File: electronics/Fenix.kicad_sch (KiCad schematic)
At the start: 9 parts, among them J1 PWR, J2 RELAY_CTRL

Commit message: Update Symbol/Footprint link & Remove GPS board
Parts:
- removed U5: (no value), Parts:Adafruit_GPSFeather, symbol Parts:Adafruit_GPSWing
- renumbered U1 to Gyro1, U3 to LoRa32_V1, U2 to Servo_Controller1, U4 to uSD1
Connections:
- net +3V3: now also TEMP_EXT1.1 (VIN), TEMP_INT1.1 (VIN); no longer TEMP_EXT1.01 (VIN), TEMP_INT1.01 (VIN)
- net GND: now also TEMP_EXT1.2 (GND), TEMP_INT1.2 (GND); no longer TEMP_EXT1.02 (GND), TEMP_INT1.02 (GND)
- net I2C_CLK: now also TEMP_EXT1.3 (SCL), TEMP_INT1.3 (SCL); no longer TEMP_EXT1.03 (SCL), TEMP_INT1.03 (SCL)
- net I2C_DATA: now also TEMP_EXT1.4 (SDA), TEMP_INT1.4 (SDA); no longer TEMP_EXT1.04 (SDA), TEMP_INT1.04 (SDA)
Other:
- note removed: "GPS & Real-Time Clock Module"

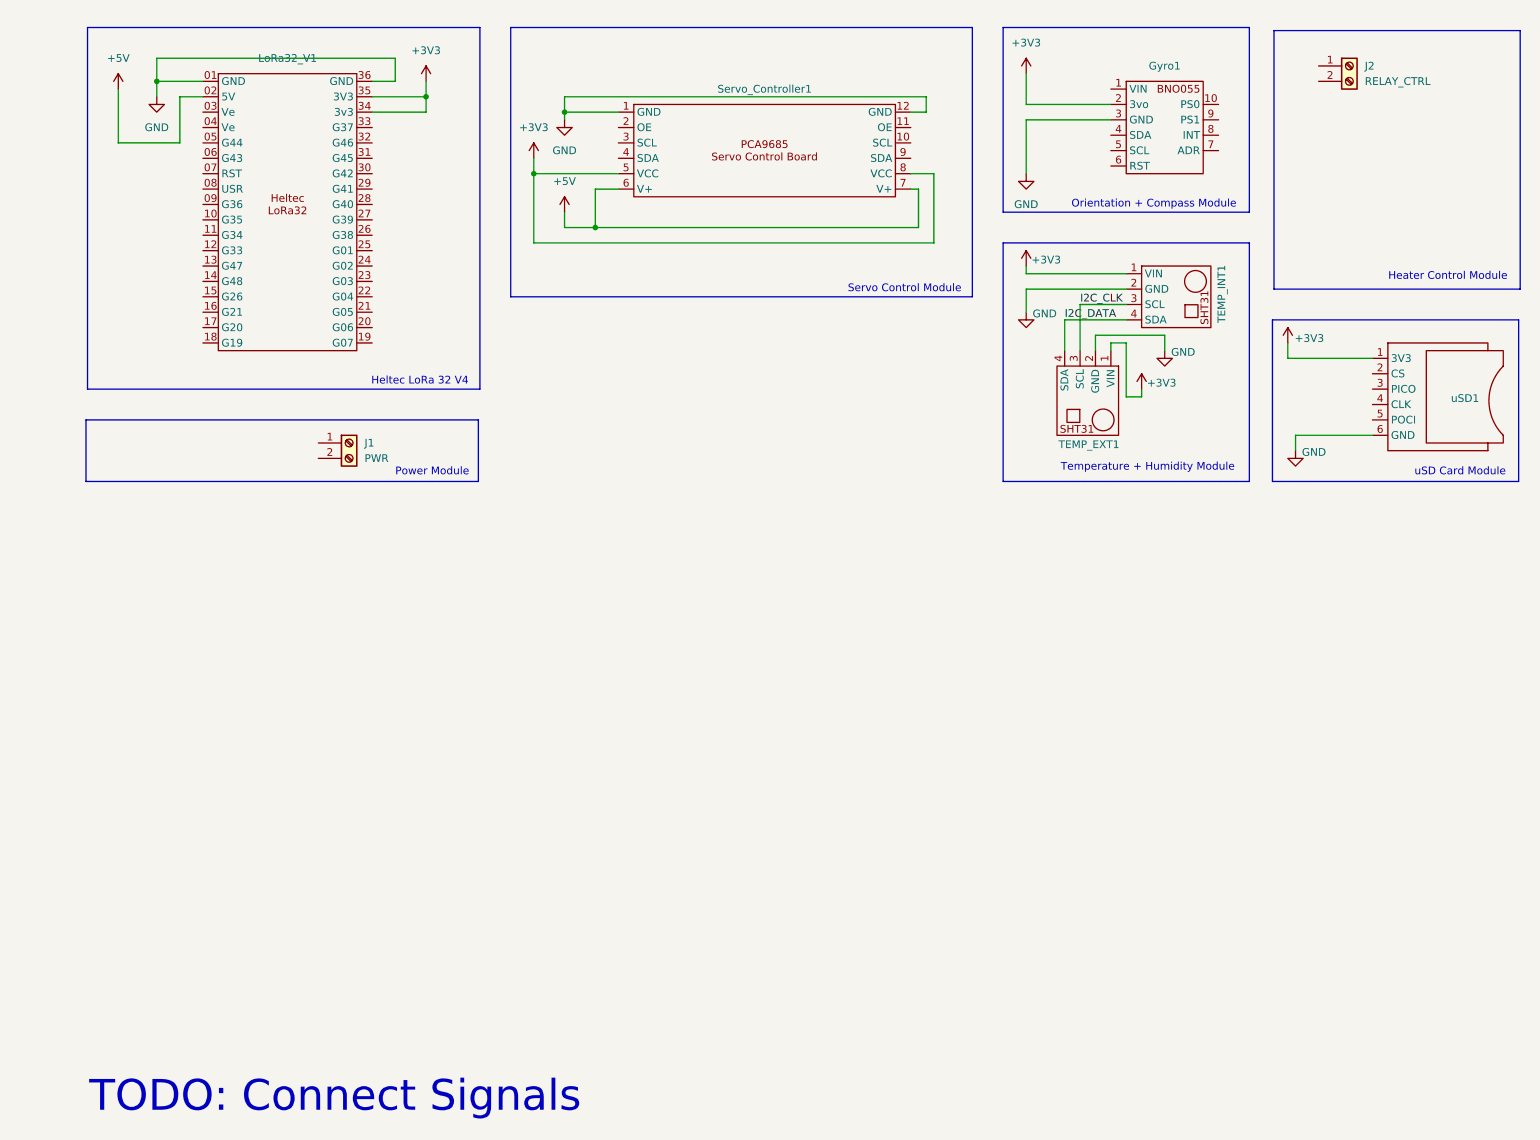
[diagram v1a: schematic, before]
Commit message: Organize nets/symbols
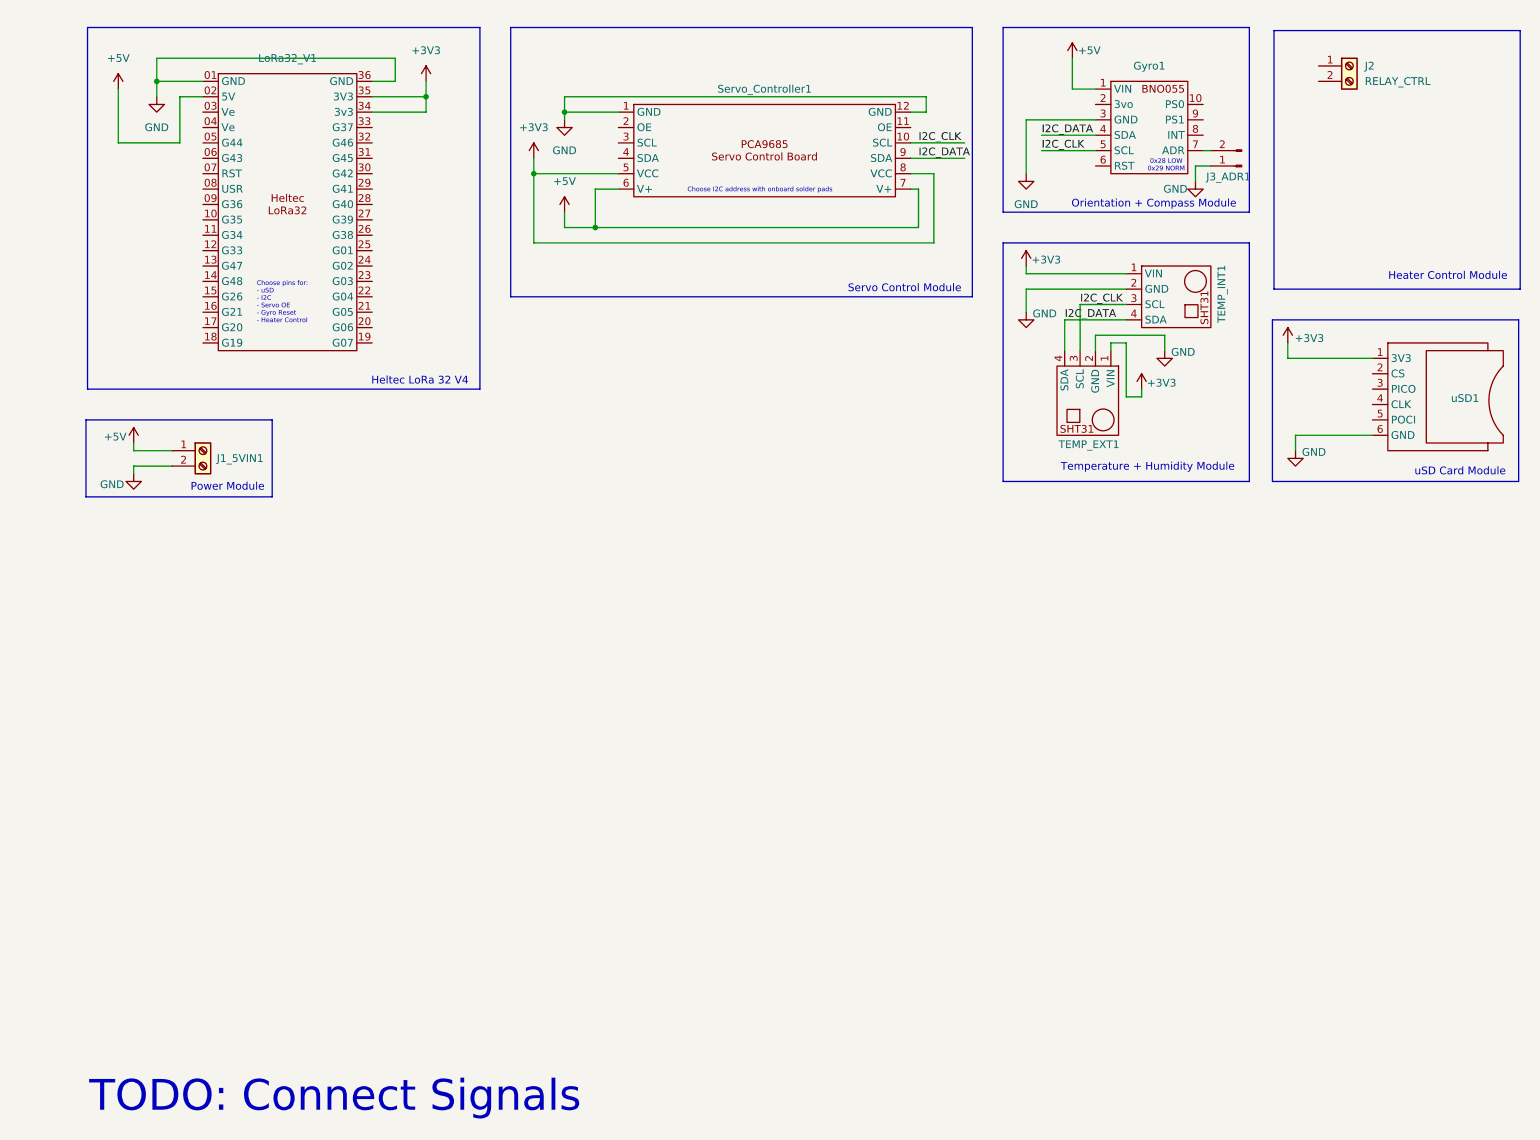
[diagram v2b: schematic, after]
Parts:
- added J3_ADR1: Conn_01x02_Pin, symbol Connector:Conn_01x02_Pin
- renumbered J1 to J1_5VIN1
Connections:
- net +3V3: no longer Gyro1.2 (3vo)
- net +5V: now also Gyro1.1 (VIN), J1_5VIN1.1 (Pin_1)
- net GND: now also J1_5VIN1.2 (Pin_2), J3_ADR1.1 (Pin_1)
- net I2C_CLK: now also Gyro1.5 (SCL), Servo_Controller1.10 (SCL)
- net I2C_DATA: now also Gyro1.4 (SDA), Servo_Controller1.9 (SDA)
- net at Gyro1.7 (ADR): now also J3_ADR1.2 (Pin_2)
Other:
- note added: "0x28 LOW 0x29 NORM"
- note added: "Choose I2C address with onboard solder pads"
- note added: "Choose pins for: - uSD - I2C - Servo OE - Gyro Reset - Heater Control"
- moved on the sheet: Gyro1, J1_5VIN1

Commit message: Hardware Night: Finish schematic and PCB routing for known parts
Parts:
- added J4_SRV_EN1: Conn_01x02_Pin, Connector_PinHeader_2.54mm:PinHeader_1x02_P2.54mm_Vertical, symbol Connector:Conn_01x02_Pin
- J3_ADR1: footprint (none) -> Connector_PinHeader_2.54mm:PinHeader_1x02_P2.54mm_Vertical
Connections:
- net GND: now also J4_SRV_EN1.2 (Pin_2)
- net I2C_CLK: now also LoRa32_V1.13 (G47), Servo_Controller1.3 (SCL)
- net I2C_DATA: now also LoRa32_V1.14 (G48), Servo_Controller1.4 (SDA)
- net SPI_CLK: now reaches LoRa32_V1.09 (G36)
- net SPI_CLK: now also uSD1.4 (CLK)
- net SPI_PICO: now reaches LoRa32_V1.10 (G35)
- net SPI_PICO: now also uSD1.3 (PICO)
- net SPI_CS_SD: now reaches LoRa32_V1.11 (G34)
- net SPI_CS_SD: now also uSD1.2 (CS)
- net GYRO_RST: now reaches LoRa32_V1.15 (G26)
- net GYRO_RST: now also Gyro1.6 (RST)
- net SPI_POCI: now reaches LoRa32_V1.33 (G37)
- net SPI_POCI: now also uSD1.5 (POCI)
- net at Servo_Controller1.11 (OE): now also J4_SRV_EN1.1 (Pin_1)
- net SERVO_EN: now reaches Servo_Controller1.2 (OE)
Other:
- note added: "Choose pins for: - Heater Control"
- note removed: "Choose pins for: - uSD - I2C - Servo OE - Gyro Reset - Heater Control"

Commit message: Update ecan, cleanup
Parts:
- removed J1_5VIN1: PWR, TerminalBlock:TerminalBlock_MaiXu_MX126-5.0-02P_1x02_P5.00mm, symbol Connector:Screw_Terminal_01x02
- added J_PWR: Conn_01x03_Pin, Connector_PinHeader_1.00mm:PinHeader_1x03_P1.00mm_Horizontal, symbol Connector:Conn_01x03_Pin
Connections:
- net +3V3: now also J_PWR.1 (Pin_1)
- net +5V: now also J_PWR.3 (Pin_3)
- net GND: now also J_PWR.2 (Pin_2)
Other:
- note added: "GPS Pins: 34 - VCC 39 - Tx (Data to Heltec) 38 - Rx 40 - Wake 41 - PPS (1Hz Pulse if GPS locked) 42 - Reset"
- note added: "LoRa Pins: 08 - NSS 09 - Clock 10 - PICO 11 - POCI 12 - Reset 13 - Busy 14 - DIO 1"

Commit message: APRS Schematic
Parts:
- added A1: RaspberryPi_Pico, Module:RaspberryPi_Pico_Common_Unspecified, symbol MCU_Module:RaspberryPi_Pico
- added C1: 100nF, Capacitor_THT:C_Disc_D4.3mm_W1.9mm_P5.00mm, symbol Device:C
- added C2: 4.7nF, Capacitor_THT:C_Disc_D4.3mm_W1.9mm_P5.00mm, symbol Device:C
- added D1, D2: 1N5817, Diode_THT:D_DO-41_SOD81_P10.16mm_Horizontal, symbol Diode:1N5817
- added J1: Radio 3.5mm, symbol Connector_Audio:AudioPlug3
- added J3: Radio 2.5mm, symbol Connector_Audio:AudioPlug3
- added J4_LORA_PWR: Conn_01x02_Pin, Connector_PinHeader_2.54mm:PinHeader_1x02_P2.54mm_Vertical, symbol Connector:Conn_01x02_Pin
- added Q1: BC548, Package_TO_SOT_THT:TO-92_Inline, symbol Transistor_BJT:BC548
- added R1, R2: 4k7, Resistor_THT:R_Axial_DIN0207_L6.3mm_D2.5mm_P7.62mm_Horizontal, symbol Device:R
- added R3: 1k, Resistor_THT:R_Axial_DIN0207_L6.3mm_D2.5mm_P7.62mm_Horizontal, symbol Device:R
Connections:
- net +5V: now also D1.2 (A), D2.2 (A); no longer LoRa32_V1.02 (5V)
- net GND: now also A1.13 (GND), A1.18 (GND), A1.23 (GND), A1.28 (GND), A1.3 (GND), A1.38 (GND), A1.8 (GND), C2.2, J3.S, Q1.3 (E), R1.2
- net APRS_TX: now reaches LoRa32_V1.19 (G07)
- net APRS_TX: now also A1.7 (GPIO5)
- net APRS_RX: now reaches LoRa32_V1.20 (G06)
- net APRS_RX: now also A1.6 (GPIO4)
- new net: Q1.2 (B), R3.1
- new net: J4_LORA_PWR.2 (Pin_2), LoRa32_V1.02 (5V)
- new net: A1.11 (GPIO8), C1.2
- new net: A1.12 (GPIO9), R3.2
- new net: A1.39 (VSYS), D1.1 (K)
- new net: C1.1, R1.1, R2.2
- new net: C2.1, J1.R, R2.1
- new net: D2.1 (K), J4_LORA_PWR.1 (Pin_1)
- new net APRS_3.5_Sleeve: J1.S, Q1.1 (C)
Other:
- note added: "APRS Modem"
- note added: "APRS UART uses UART2"
- note added: "Hardware follows design of eleccoder/raspi-pico-aprs-tnc"
- note added: "Power board from 5v if not using onboard battery manager"
- note added: "SPI OK on both SPI1/SPI2"
- note removed: "TODO: Connect Signals"

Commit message: APRS Footprints
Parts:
- J1: footprint (none) -> Parts:TRS_3.5mm
- J3: footprint (none) -> Parts:TRS_2.5mm
- renumbered J4_LORA_PWR to J4_LORA_PWR1, J_PWR to J_PWR1
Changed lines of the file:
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@@
 		(dnp no)
 		(fields_autoplaced yes)
-		(property "Reference" "J_PWR"
+		(property "Reference" "J_PWR1"
 			(at 38.1 91.4399 0)
 			(show_name no)
@@
 			(project ""
 				(path "/cfd0b8a8-74a1-487b-95ef-a5983af16f57"
-					(reference "J_PWR")
+					(reference "J_PWR1")
 					(unit 1)
 				)
@@
 			)
 		)
-		(property "Footprint" ""
+		(property "Footprint" "Parts:TRS_2.5mm"
 			(at 106.68 91.44 0)
 			(hide yes)
@@
 			)
 		)
-		(property "Footprint" ""
+		(property "Footprint" "Parts:TRS_3.5mm"
 			(at 93.98 91.44 0)
 			(hide yes)
@@
 		(in_pos_files yes)
 		(dnp no)
-		(property "Reference" "J4_LORA_PWR"
+		(property "Reference" "J4_LORA_PWR1"
 			(at 32.004 42.418 0)
 			(show_name no)
@@
 			(project "Fenix"
 				(path "/cfd0b8a8-74a1-487b-95ef-a5983af16f57"
-					(reference "J4_LORA_PWR")
-					(unit 1)
-				)
+					(reference "J4_LORA_PWR1")
+					(unit 1)
+				)

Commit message: Pre-Routing Board Layout
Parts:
- removed J2: RELAY_CTRL, TerminalBlock:TerminalBlock_MaiXu_MX126-5.0-02P_1x02_P5.00mm, symbol Connector:Screw_Terminal_01x02
- removed J_PWR1: Conn_01x03_Pin, Connector_PinHeader_1.00mm:PinHeader_1x03_P1.00mm_Horizontal, symbol Connector:Conn_01x03_Pin
- added J2: Relay_Control, Connector_Phoenix_MSTB:PhoenixContact_MSTBVA_2,5_3-G_1x03_P5.00mm_Vertical, symbol Connector:Conn_01x03_Pin
- added J4: PWR_MON, Connector_PinHeader_2.54mm:PinHeader_2x02_P2.54mm_Vertical, symbol Connector_Generic:Conn_02x02_Counter_Clockwise
- added J5: PWR_IN, TerminalBlock_Altech:Altech_AK100_1x02_P5.00mm, symbol Connector:Screw_Terminal_01x02
- added REG1: (no value), symbol Parts:5V_REG
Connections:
- net +3V3: now also J2.3 (Pin_3), J4.4 (Pin_4)
- net +5V: now also J4.1 (Pin_1), REG1.4 (5V_OUT)
- net GND: now also J2.1 (Pin_1), J4.2 (Pin_2), J5.2 (Pin_2), REG1.1 (GND_IN), REG1.3 (GND_OUT)
- net RELAY_EN: now reaches LoRa32_V1.23 (G03)
- net RELAY_EN: now also J2.2 (Pin_2)
- new net: J4.3 (Pin_3), J5.1 (Pin_1), REG1.2 (5-30V_IN)
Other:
- note removed: "Choose pins for: - Heater Control"
- moved on the sheet: uSD1
